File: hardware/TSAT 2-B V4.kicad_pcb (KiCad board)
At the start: 2 copper layers, 84.5 x 75 mm, 17 parts

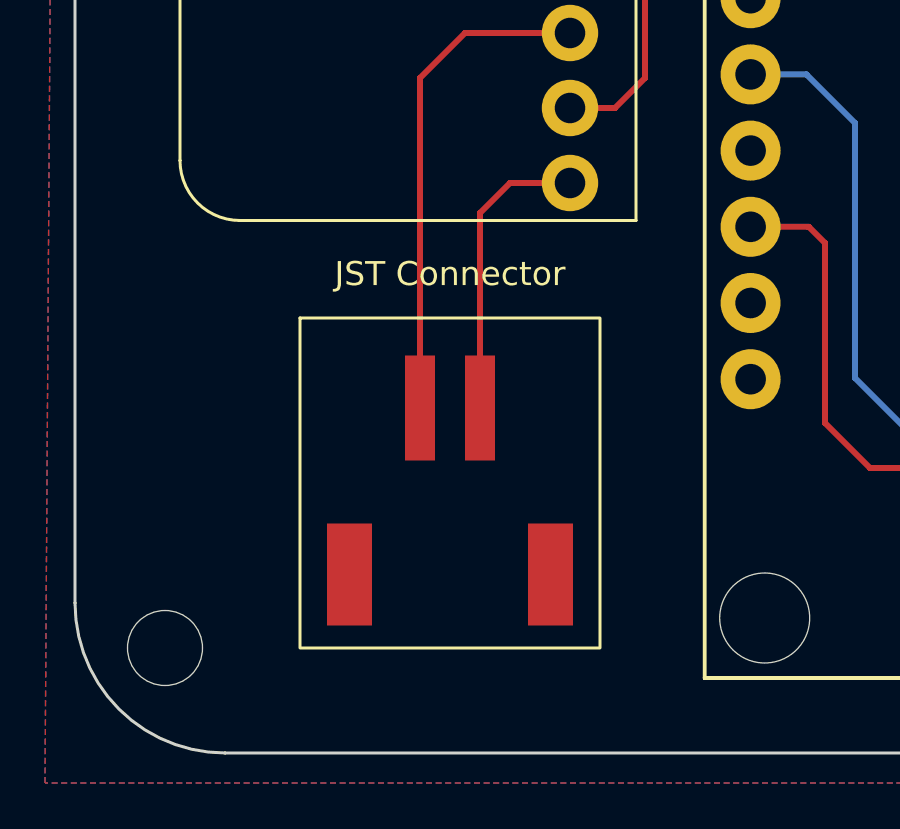
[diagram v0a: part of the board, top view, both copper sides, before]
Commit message: Updated PCB with correct JST connector
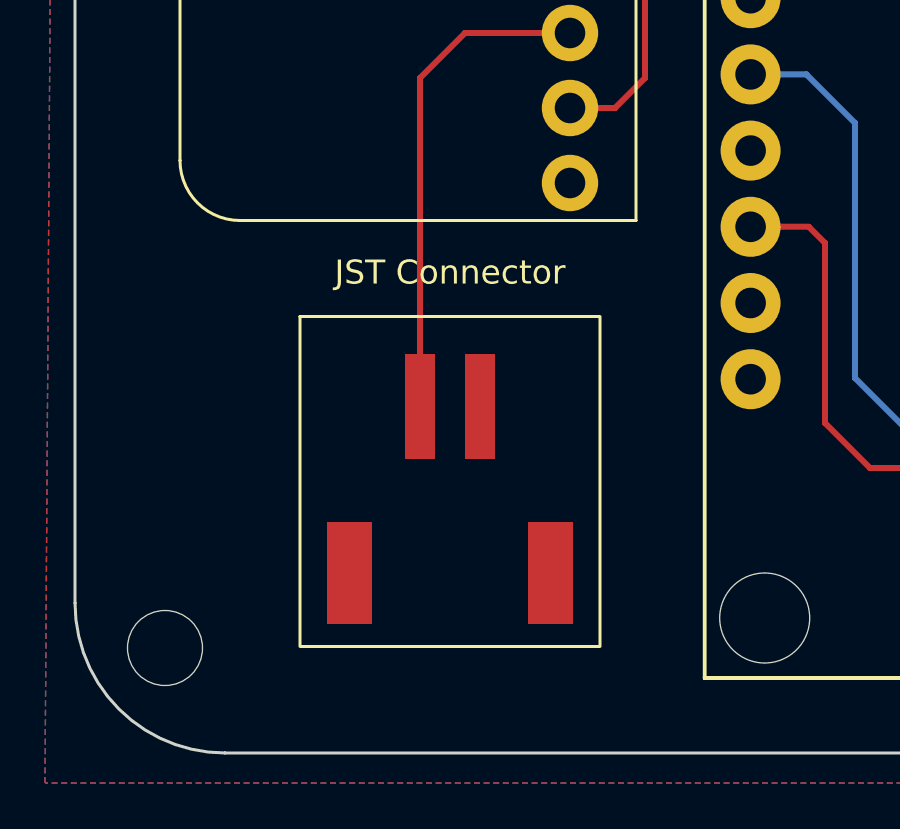
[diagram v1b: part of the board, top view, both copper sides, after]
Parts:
- moved REF** 0.05 mm to (77.5, 137.4)
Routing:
- net GND: track 9.91 -> 0.00 mm
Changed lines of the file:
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@@
 	(footprint "TSAT2-B PCB Footprints:JST-PH 2-Pin SMT Right Angle Connector"
 		(layer "F.Cu")
-		(at 77.5 137.5)
+		(at 77.5 137.45)
 		(property "Reference" "REF**"
 			(at 0 -0.5 0)
@@
 			(layers "F.Cu" "F.Mask" "F.Paste")
 			(net 12 "5V")
-			(solder_mask_margin 0.05)
-			(clearance 0.1)
 		)
 		(pad "2" smd rect
@@
 			(layers "F.Cu" "F.Mask" "F.Paste")
 			(net 2 "GND")
-			(solder_mask_margin 0.05)
-			(clearance 0.1)
 		)
 		(pad "3" smd rect
@@
 			(size 1.5 3.4)
 			(layers "F.Cu" "F.Mask" "F.Paste")
-			(solder_mask_margin 0.05)
-			(clearance 0.1)
 		)
 		(pad "4" smd rect
@@
 			(size 1.5 3.4)
 			(layers "F.Cu" "F.Mask" "F.Paste")
-			(solder_mask_margin 0.05)
-			(clearance 0.1)
 		)
 		(embedded_fonts no)
@@
 	)
 	(segment
-		(start 77.5 137.5)
-		(end 77.5 131)
-		(width 0.2)
-		(layer "F.Cu")
-		(net 2)
-	)
-	(segment
-		(start 77.5 131)
-		(end 78.5 130)
-		(width 0.2)
-		(layer "F.Cu")
-		(net 2)
-	)
-	(segment
-		(start 78.5 130)
-		(end 80.5 130)
-		(width 0.2)
-		(layer "F.Cu")
-		(net 2)
-	)
-	(segment
 		(start 136.5 137)
 		(end 134 139.5)
@@
 			)
 		)
-	)
-	(zone
-		(net 0)
-		(net_name "")
-		(layers "F.Cu" "B.Cu")
-		(name "JST connector")
-		(hatch edge 0.5)
-		(connect_pads
-			(clearance 0)
-		)
-		(min_thickness 0.25)
-		(filled_areas_thickness no)
-		(keepout
-			(tracks allowed)
-			(vias allowed)
-			(pads allowed)
-			(copperpour not_allowed)
-			(footprints allowed)
-		)
-		(placement
-			(enabled no)
-			(sheetname "")
-		)
-		(fill
-			(thermal_gap 0.5)
-			(thermal_bridge_width 0.5)
-		)
-		(polygon
-			(pts
-				(xy 81.5 145.5) (xy 71.5 145.5) (xy 71.5 134.5) (xy 81.5 134.5)
-			)
-		)
